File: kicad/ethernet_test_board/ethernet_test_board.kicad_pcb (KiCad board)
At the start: 2 copper layers, 100 x 100 mm, 0 parts

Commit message: [add] kicad sch (finish) kicad pcb (WIP)
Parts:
- added C1: 10nF, Capacitor_SMD:C_0603_1608Metric, F.Cu at (138.7, 54.4)
- added C10: 6.8n, Capacitor_SMD:C_0603_1608Metric, F.Cu at (134.6, 78.7)
- added C11: 6.8n, Capacitor_SMD:C_0603_1608Metric, F.Cu at (136.1, 78.7)
- added C12: 10n, Capacitor_SMD:C_0603_1608Metric, F.Cu at (134.0, 73.6)
- added C13: 18p, Capacitor_SMD:C_0603_1608Metric, F.Cu at (133.1, 51.3)
- added C14: 18p, Capacitor_SMD:C_0603_1608Metric, F.Cu at (135.7, 46.8)
- added C15: 1μ, Capacitor_SMD:C_0603_1608Metric, F.Cu at (122.8, 64.4)
- added C16: 1μ, Capacitor_SMD:C_0603_1608Metric, F.Cu at (126.0, 66.7)
- added C17: C, Capacitor_SMD:C_0603_1608Metric_Pad1.08x0.95mm_HandSolder, F.Cu at (151.5, 50.5)
- added C18: C, Capacitor_SMD:C_0603_1608Metric_Pad1.08x0.95mm_HandSolder, F.Cu at (130.8, 69.4)
- added C19: C, Capacitor_SMD:C_0603_1608Metric_Pad1.08x0.95mm_HandSolder, F.Cu at (134.5, 69.6)
- added C2: 10μ, Capacitor_SMD:C_0603_1608Metric, F.Cu at (124.3, 59.5)
- added C20: C, Capacitor_SMD:C_0603_1608Metric_Pad1.08x0.95mm_HandSolder, F.Cu at (140.9, 55.3)
- added C21: C, Capacitor_SMD:C_0603_1608Metric_Pad1.08x0.95mm_HandSolder, F.Cu at (156.6, 50.5)
- added C3: 10μ, Capacitor_SMD:C_0603_1608Metric, F.Cu at (127.6, 60.3)
- added C4: 4.7μ, Capacitor_SMD:C_0603_1608Metric, F.Cu at (140.6, 58.5)
- added C5: 0.1μ, Capacitor_SMD:C_0603_1608Metric, F.Cu at (145.4, 70.5)
- added C6: 0.1u, Capacitor_SMD:C_0603_1608Metric, F.Cu at (142.4, 55.9)
- added C7: 10μ, Capacitor_SMD:C_0603_1608Metric, F.Cu at (142.4, 70.5)
- added C8: 15p, Capacitor_SMD:C_0603_1608Metric, F.Cu at (145.0, 58.4)
- added C9: 22n, Capacitor_SMD:C_0603_1608Metric, F.Cu at (137.6, 81.0)
- added D1: LED, Capacitor_SMD:C_0603_1608Metric, F.Cu at (151.4, 46.9)
- added D2: LED, Capacitor_SMD:C_0603_1608Metric, F.Cu at (151.4, 48.4)
- added D3: D, Capacitor_SMD:C_0603_1608Metric_Pad1.08x0.95mm_HandSolder, F.Cu at (120.9, 53.8)
- added D4: LED, LED_SMD:LED_0603_1608Metric, F.Cu at (162.4, 79.0)
- added J1: USB_C_Receptacle_USB2.0_16P, Connector_USB:USB_C_Receptacle_GCT_USB4105-xx-A_16P_TopMnt_Horizontal, B.Cu at (129.0, 50.2)
- added J2: Conn_01x02_Pin, ILG:ILG2pin, F.Cu at (161.8, 54.5)
- added J3: TMJD4152NENLC, TMJD4152NENLC:TMJD4152NENLC, B.Cu at (141.5, 81.4)
- added J4: Conn_02x13_Top_Bottom, Connector_PinHeader_2.54mm:PinHeader_2x13_P2.54mm_Vertical, B.Cu at (119.1, 58.3)
- added J5: TMJD4152NENLC, TMJD4152NENLC:TMJD4152NENLC, B.Cu at (137.3, 92.8)
- added J7: Micro_SD_Card_Det_Hirose_DM3AT, Connector_Card:microSD_HC_Hirose_DM3AT-SF-PEJM5, F.Cu at (155.7, 70.4)
- added J8: Conn_01x02_Pin, Connector_JST:JST_VH_B2P-VH-B_1x02_P3.96mm_Vertical, B.Cu at (121.2, 50.2)
- added R1: 1k, Capacitor_SMD:C_0603_1608Metric, F.Cu at (127.8, 62.6)
- added R10: 10K, Resistor_SMD:R_0603_1608Metric, F.Cu at (145.4, 73.5)
- added R11: 10K, Resistor_SMD:R_0603_1608Metric, F.Cu at (141.2, 72.0)
- added R12: 10K, Resistor_SMD:R_0603_1608Metric, F.Cu at (139.2, 68.8)
- added R13: 10K, Resistor_SMD:R_0603_1608Metric, F.Cu at (144.3, 68.7)
- added R14: 10K, Resistor_SMD:R_0603_1608Metric, F.Cu at (143.0, 67.3)
- added R15: 100, Resistor_SMD:R_0603_1608Metric, F.Cu at (159.4, 79.0)
- added R16: 49.9, Capacitor_SMD:C_0603_1608Metric, F.Cu at (141.6, 78.7)
- added R17: 49.9, Capacitor_SMD:C_0603_1608Metric, F.Cu at (143.1, 78.8)
- added R19: 10, Capacitor_SMD:C_0603_1608Metric, F.Cu at (138.3, 78.8)
- added R2: R, Capacitor_SMD:C_0603_1608Metric, F.Cu at (141.0, 60.1)
- added R20: 49.9, Capacitor_SMD:C_0603_1608Metric, F.Cu at (134.6, 75.8)
- added R21: 49.9, Capacitor_SMD:C_0603_1608Metric, F.Cu at (136.1, 75.8)
- added R22: 1M, Capacitor_SMD:C_0603_1608Metric, F.Cu at (136.1, 51.3)
- added R23: R, Capacitor_SMD:C_0603_1608Metric, F.Cu at (154.4, 46.9)
- added R24: R, Capacitor_SMD:C_0603_1608Metric, F.Cu at (154.4, 48.4)
- added R3: R, Capacitor_SMD:C_0603_1608Metric, F.Cu at (122.4, 56.5)
- added R4: 5.1k, Capacitor_SMD:C_0603_1608Metric, F.Cu at (129.9, 51.6)
- added R5: 5.1k, Capacitor_SMD:C_0603_1608Metric, F.Cu at (128.1, 51.6)
- added R6: 12.4k, Capacitor_SMD:C_0603_1608Metric, F.Cu at (135.9, 71.1)
- added R7: 10k, Resistor_SMD:R_0603_1608Metric, F.Cu at (159.0, 59.2)
- added R8: 1k, Resistor_SMD:R_0603_1608Metric, F.Cu at (147.3, 56.2)
- added R9: 10K, Resistor_SMD:R_0603_1608Metric, F.Cu at (145.4, 76.4)
- added SW1: SW_Push, Button_Switch_THT:SW_PUSH_6mm_H7.3mm, B.Cu at (146.0, 47.7)
- added SW2: SW_Push, Button_Switch_THT:SW_PUSH_6mm_H7.3mm, B.Cu at (122.4, 76.9)
- added U1: W55RP20, W55RP20:QFN40P800X800X90-69N, F.Cu at (134.5, 61.3)
- added U2: RT9080, Package_TO_SOT_SMD:TSOT-23-5, F.Cu at (124.2, 62.0)
- added U3: MCP25625-x-SS, Package_SO:SSOP-28_5.3x10.2mm_P0.65mm, F.Cu at (152.8, 56.7)
- added U4: XC6201, Package_TO_SOT_SMD:SOT-23-5, F.Cu at (123.2, 66.8)
- added U5: SiT2001B, Package_TO_SOT_SMD:SOT-23-5, F.Cu at (144.9, 55.6)
- added U6: LM66100DCKR, LM66100DCKR:SOT65P210X110-6N, F.Cu at (125.0, 57.3)
- added Y1: FA-128, Oscillator:Oscillator_SMD_SeikoEpson_SG210-4Pin_2.5x2.0mm, F.Cu at (135.8, 49.1)
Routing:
- net +3.3V: track 0.00 -> 105.0 mm, vias 0 -> 7
- net /SPEED: track 0.00 -> 67.8 mm, vias 0 -> 1
- net +5V: track 0.00 -> 67.3 mm, vias 0 -> 2
- net /TXM: track 0.00 -> 55.6 mm, vias 0 -> 2
- net /TXP: track 0.00 -> 55.0 mm, vias 0 -> 2
- net GND: track 0.00 -> 51.8 mm, vias 0 -> 22
- net /Ethernet_PoE: track 0.00 -> 44.4 mm
- net /SWD: track 0.00 -> 42.6 mm, vias 0 -> 1
- net /SWCLK: track 0.00 -> 39.1 mm, vias 0 -> 1
- net /RXP: track 0.00 -> 39.0 mm, vias 0 -> 1
- net Net-(J3-CT_2): track 0.00 -> 38.4 mm, vias 0 -> 1
- net /RXM: track 0.00 -> 36.4 mm, vias 0 -> 1
- net /GPIO16: track 0.00 -> 33.7 mm, vias 0 -> 1
- net /GPIO15: track 0.00 -> 30.6 mm, vias 0 -> 1
- net /GPIO18: track 0.00 -> 26.1 mm, vias 0 -> 1
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- added copper zone on F.Cu, net +5V
- added copper zone on B.Cu, net GND
- added copper zone on F.Cu, net GND
- added copper zone on In1.Cu, net GND
- added copper zone on In2.Cu, net GND
- added copper zone on In3.Cu, net GND
- added copper zone on In4.Cu, net GND
- added copper zone on In5.Cu, net GND
- added copper zone on In6.Cu, net GND
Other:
- board size 100 x 100 mm -> 50 x 50 mm
- copper layers 2 -> 8

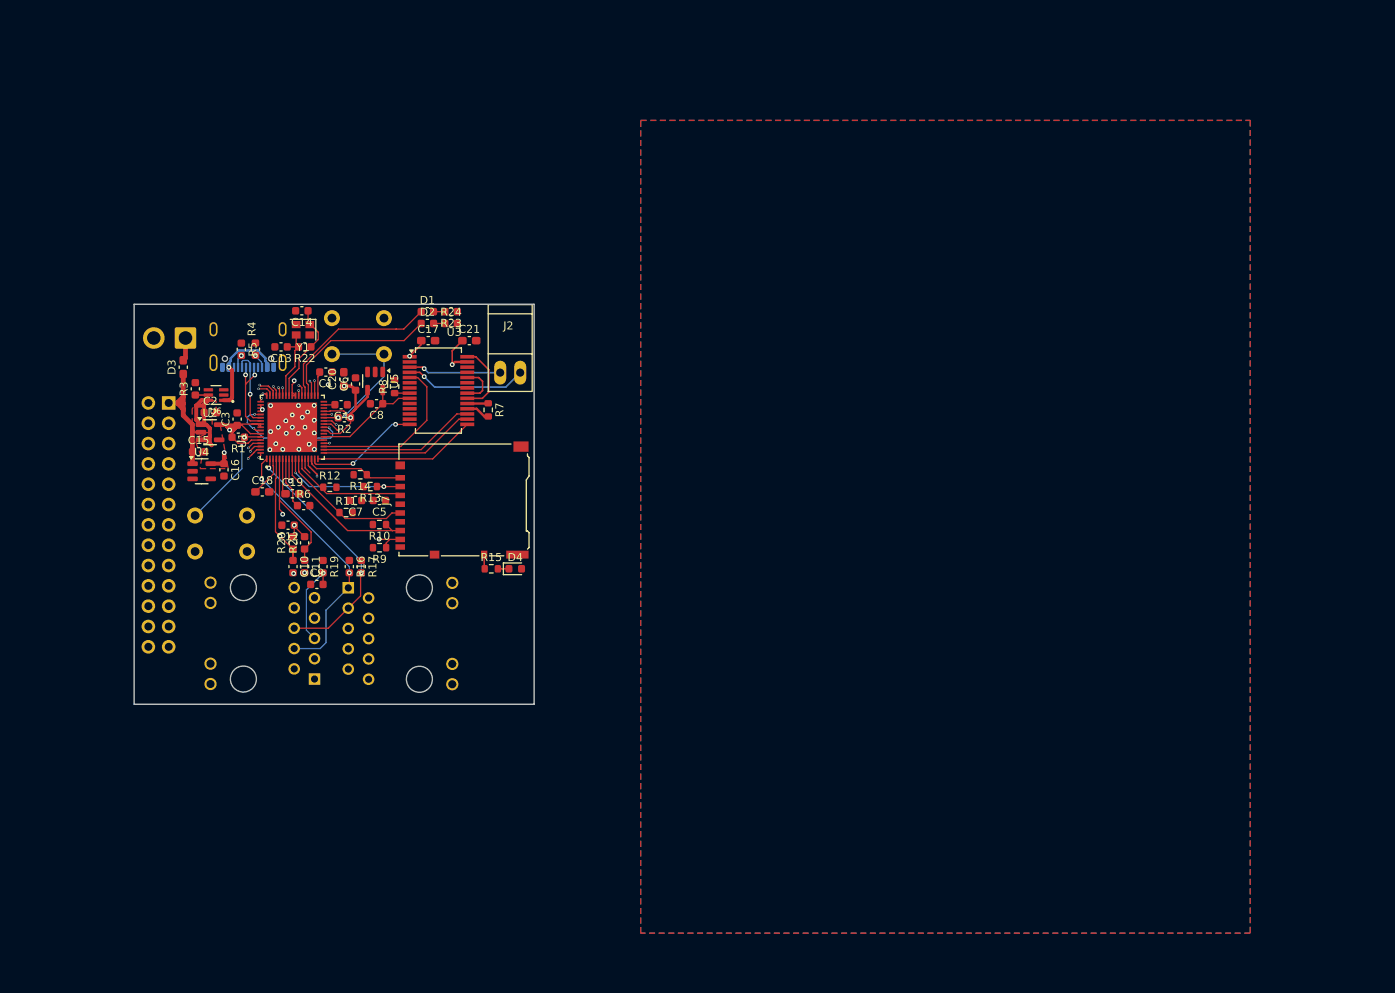
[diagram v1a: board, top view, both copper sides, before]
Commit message: [fix] kicad ethernet error
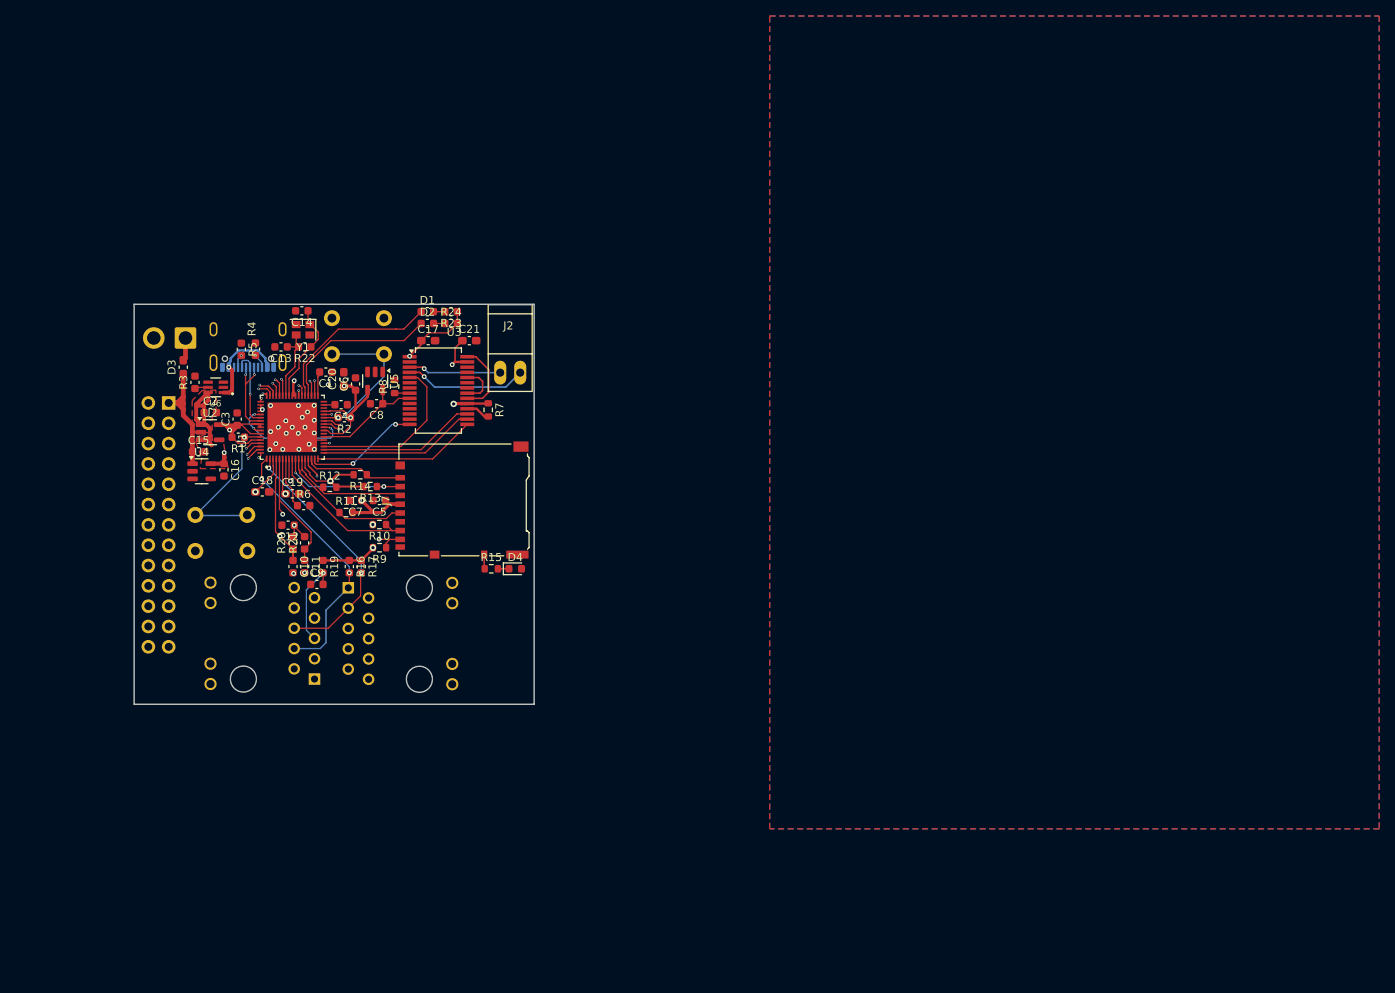
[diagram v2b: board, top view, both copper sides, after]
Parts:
- moved U6 0.96 mm to (124.9, 56.3)
- moved R3 0.81 mm to (122.3, 55.7)
- moved SW2 0.08 mm to (122.4, 76.8)
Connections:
- R16 pad 1: +3.3VA -> +3.3V
- R17 pad 1: +3.3VA -> +3.3V
- R19 pad 1: +3.3VA -> +3.3V
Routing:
- net +3.3V: track 105.0 -> 190.9 mm, vias 7 -> 14
- net Net-(U1-BOOT): track 14.4 -> 20.9 mm
- net /GPIO27: track 22.3 -> 24.7 mm
- net /GPIO26: track 22.6 -> 24.7 mm
- net +5V: track 67.3 -> 68.7 mm
- net /USB_VCC: track 12.8 -> 11.8 mm
- net /GPIO28: track 19.9 -> 20.8 mm
- net GND: vias 22 -> 21
- net /TXM: vias 2 -> 3

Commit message: [add] kicad pcb
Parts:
- moved D4 3.34 mm to (159.4, 80.5), turned to 180 degrees
- moved D3 2.64 mm to (118.5, 55.0)
- moved R2 0.91 mm to (141.9, 59.8)
- moved R3 0.70 mm to (121.7, 55.8), turned to 180 degrees
- moved C6 0.60 mm to (142.4, 55.3)
- moved C1 0.40 mm to (138.7, 54.0)
- moved C4 0.38 mm to (140.7, 58.1)
- moved R8 0.34 mm to (147.3, 56.6)
- moved R9 0.31 mm to (145.4, 76.7)
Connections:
- U6 pad 3: GND -> +5V
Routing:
- net /LINK: track 1.91 -> 87.1 mm, vias 1 -> 3
- net +3.3V: track 190.9 -> 246.1 mm, vias 14 -> 19
- net GND: track 51.8 -> 89.2 mm, vias 21 -> 236
- net +BATT: track 15.8 -> 12.2 mm
- net Net-(U1-BOOT): track 20.9 -> 24.3 mm
- net +5V: track 68.7 -> 71.6 mm
- net Net-(D3-A): track 2.90 -> 5.04 mm, vias 0 -> 1
- net /SWD: track 42.7 -> 43.5 mm
- net /GPIO26: track 24.7 -> 25.5 mm
- net /SWCLK: track 39.2 -> 40.0 mm
- net /GPIO16: track 33.5 -> 34.3 mm
- net /PMODE0: track 15.5 -> 14.7 mm
- net /GPIO2: track 19.4 -> 20.2 mm
- net /USB_VCC: track 11.8 -> 11.2 mm
- net /GPIO29: track 21.3 -> 21.9 mm
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
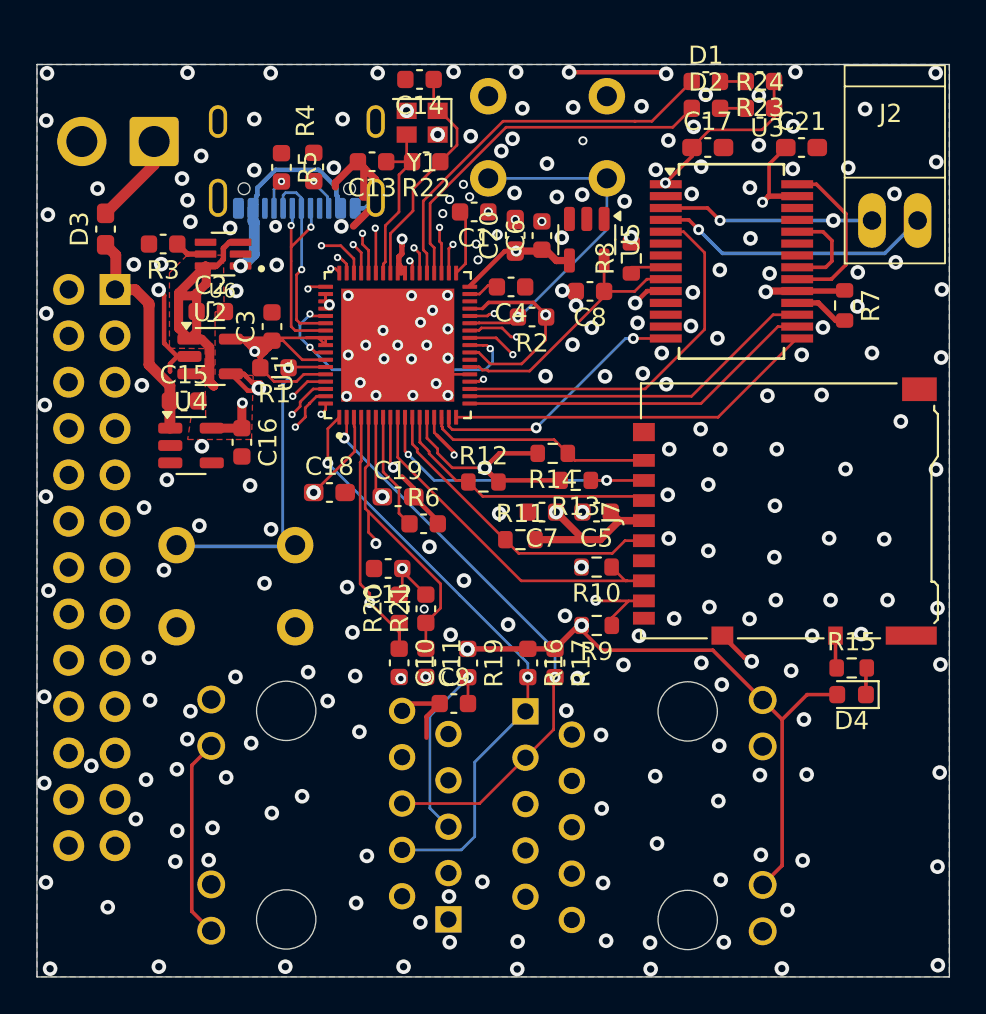
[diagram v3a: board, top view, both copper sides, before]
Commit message: [fix] fix pcb error
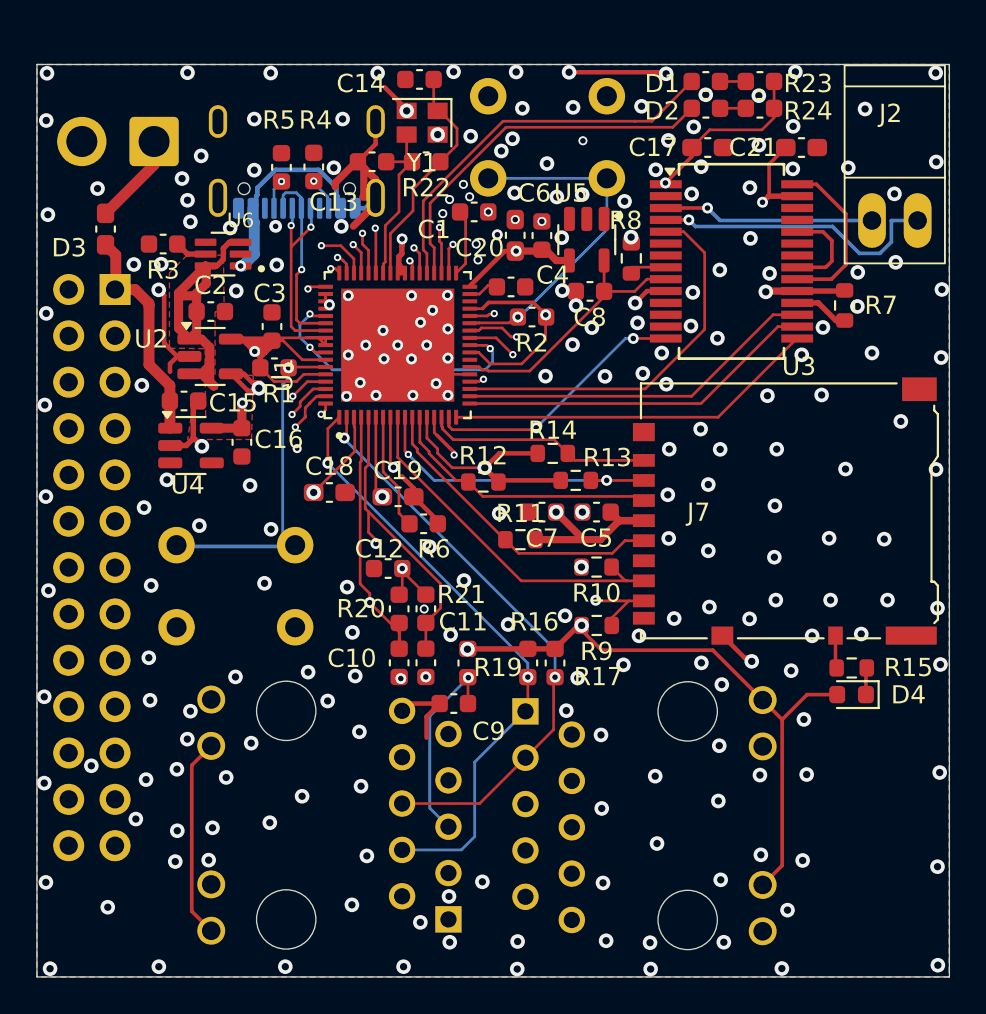
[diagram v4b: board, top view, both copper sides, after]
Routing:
- net GND: track 89.2 -> 97.8 mm, vias 236 -> 238
- net Net-(J2-Pin_2): track 15.3 -> 16.0 mm
- net Net-(J3-RD-): track 24.5 -> 25.1 mm
- net /LINK: track 87.1 -> 87.7 mm
- net Net-(J2-Pin_1): vias 2 -> 1

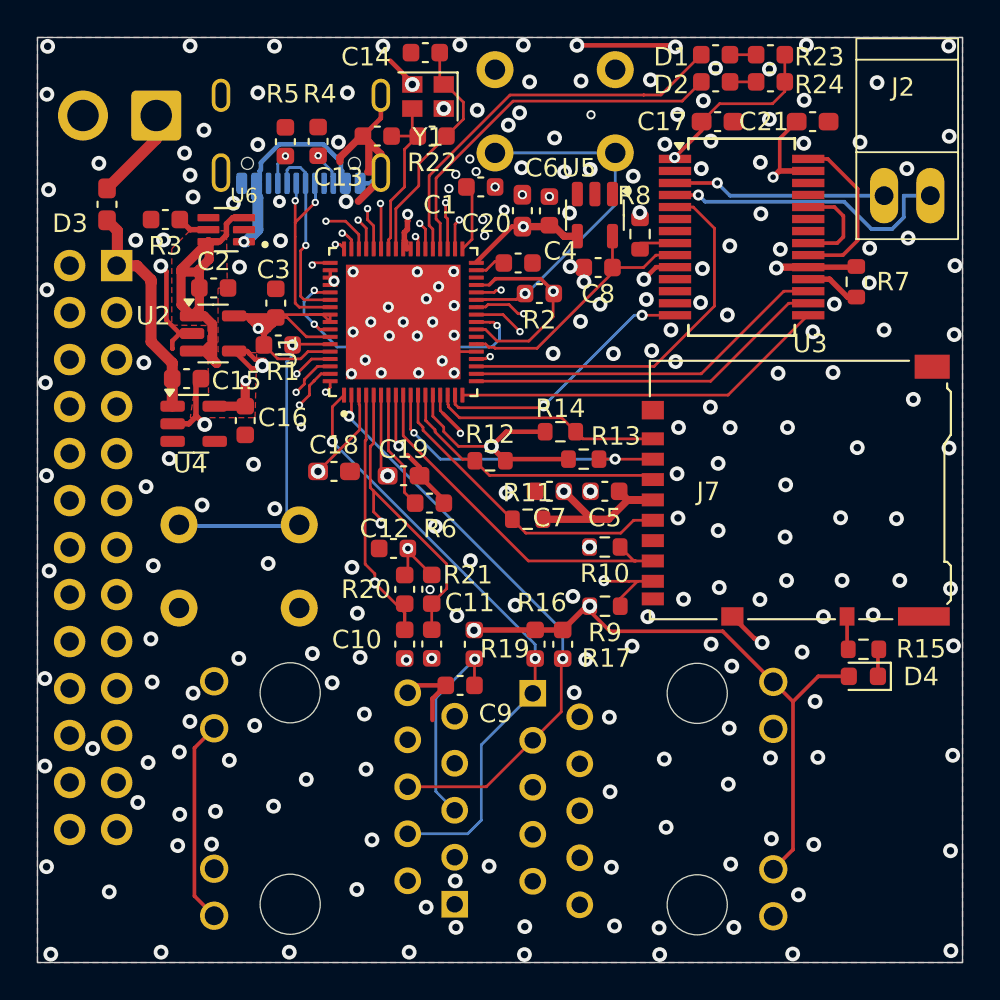
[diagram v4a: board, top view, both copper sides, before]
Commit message: [fix] via size
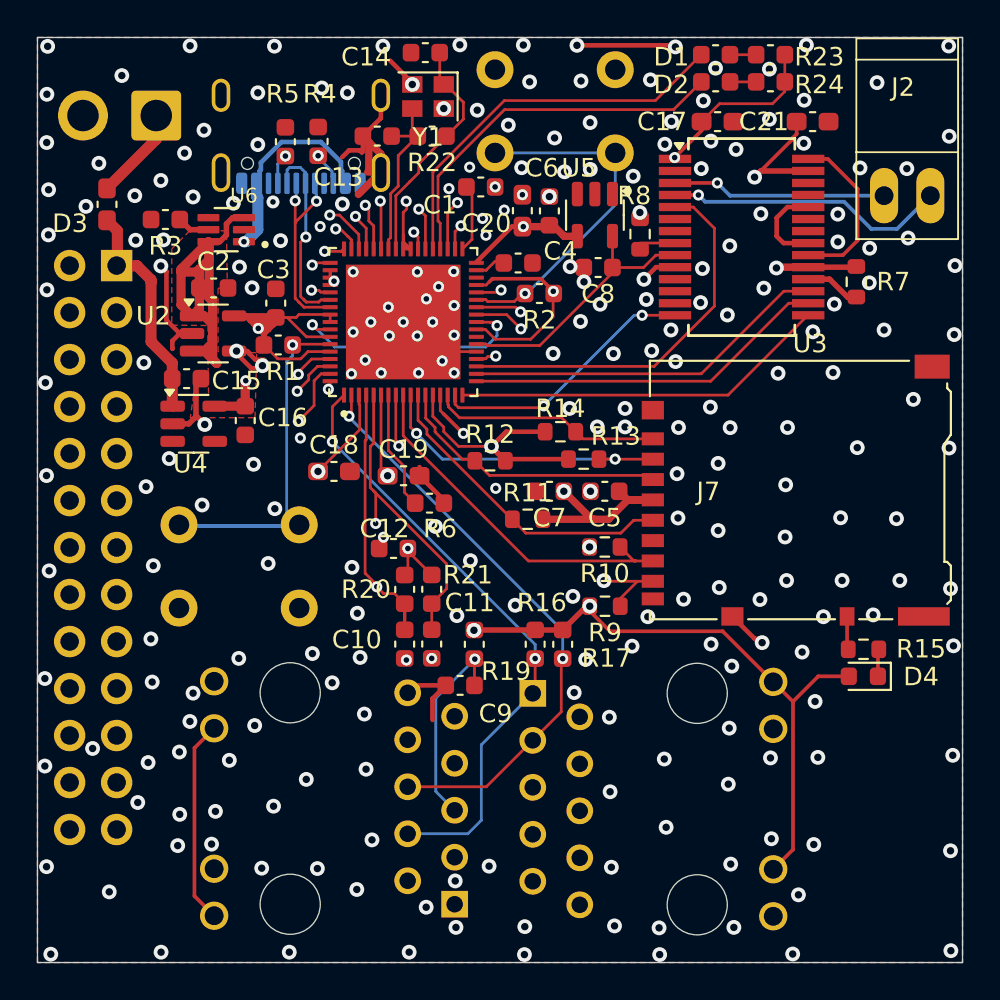
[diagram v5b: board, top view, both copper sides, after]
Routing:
- net +5V: track 71.6 -> 77.0 mm
- net /GPIO18: track 26.1 -> 27.7 mm
- net /DAT1: track 18.9 -> 17.8 mm
- net GND: track 97.8 -> 96.8 mm, vias 238 -> 247
- net Net-(J2-Pin_2): track 16.0 -> 15.3 mm
- net Net-(U3-RxCAN): track 5.31 -> 4.80 mm
- net /LINK: track 87.7 -> 87.2 mm, vias 3 -> 1
- net +3.3V: track 246.1 -> 246.4 mm, vias 19 -> 15
- net /SPEED: track 67.5 -> 67.2 mm, vias 3 -> 1
- net Net-(U1-RUN): track 18.9 -> 19.0 mm, vias 3 -> 1
- net /Ethernet_PoE: vias 2 -> 0
- net unconnected-(J5-NC-Pad8): vias 1 -> 0
- net unconnected-(J3-NC-Pad8): vias 1 -> 0
- net Net-(J3-RD-): vias 3 -> 1
- net Net-(J3-RD+): vias 3 -> 1
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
